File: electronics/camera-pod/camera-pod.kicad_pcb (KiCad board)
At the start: 2 copper layers, 40 x 27 mm, 16 parts, among them J1 LEAD, J2 MEGA, U1 AMS1117-3.3

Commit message: Schematic review S1, S4, S6: POS_IN 150k, the hub's ON LEDs on 18k, the camera's 0.75 A PTC
The user approved them ("S1 oui / S6 oui / S4 oui").

* S1, bay node: R29 470k -> 150k (C22807, basic).
  - Before its firmware runs, the upstream POS output (a node's IO42, the
    hub's IO10-13) floats. The BAT54S's warm leakage (about 2-3 uA at
    65 C) could then lift POS_IN through 470k to VIL.
  - Driven high through R30 + R28, 150k still gives 2.87 V, above VIH.
  - The design.py notes and bay_node.dtsi follow.
* S4, power hub: R41-R44 (the ON LEDs on the row outputs) 10k -> 18k
  (C25810, already on the board): 1.4 mA and 37 mW at 28 V. The 10k
  ran at 75 % of its 0603 rating at 29.4 V.
* S6, bay node: F1 (CAM_5V) goes from the 0.5 A PTC to SMD1206P075TF
  (RUILON, C20987, new catalog key pptc750): 0.75 A hold, 1.5 A trip,
  the same 1206 footprint. It is extended like C20799, so no fee changes.
  - Arducam gives the Mega 317 mA working: with the LEDs that is
    ~0.42 A on CAM_5V, where the 0.5 A part holds ~0.31 A at 70 C.
  - The camera pod's LDO tab gets the copper its routing leaves: a
    top-side +3V3 pour round the tab and a bottom-side island, joined by
    three vias. U1 drops ~0.5 W at 317 mA. The routing is unchanged.
  - The "~120 mA" notes go to 317 mA (node and pod design.py,
    electronics.md).
  - The bay's worst case follows: <= 2.25 A on +5V, the buck's inductor
    peaking at ~2.65 A (under its 2.9 A minimum limit), 13.5 W from
    VRACK (power-distribution-review.md, the buck notes).

The routed PCBs keep their routing.
- Node and hub: only the changed parts' properties (KiCad's Python, as
  pcbgen sets them).
- Pod: the two new zones and three vias, refilled.
- ERC 0, DRC 0, unconnected 0, parity 0 on all three (run on the Mac:
  zephyrbox didn't answer).
- keep_unchanged kept the node's renders and the hub's Gerbers. The
  hub's bottom render is restored: 9 pixels of via-hole noise, as before.
- The pod's renders, Gerbers and viewer GLB chang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
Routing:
- net +3V3: vias 0 -> 3
- added copper zone on B.Cu, net +3V3
- added copper zone on F.Cu, net +3V3
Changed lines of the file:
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@@
+	)
+	(via
+		(at 24.75 12.6)
+		(size 0.6)
+		(drill 0.3)
+		(layers "F.Cu" "B.Cu")
+		(locked yes)
+		(free yes)
+		(net "+3V3")
+	)
+	(via
+		(at 24.75 14.6)
+		(size 0.6)
+		(drill 0.3)
+		(layers "F.Cu" "B.Cu")
+		(locked yes)
+		(free yes)
+		(net "+3V3")
+	)
+	(via
+		(at 24.75 13.6)
+		(size 0.6)
+		(drill 0.3)
+		(layers "F.Cu" "B.Cu")
+		(locked yes)
+		(free yes)
+		(net "+3V3")
 	)
 	(via
@@
 			)
 		)
+	)
+	(zone
+		(net "+3V3")
+		(layer "F.Cu")
+		(name "ldo-tab")
+		(hatch edge 0.5)
+		(priority 2)
+		(connect_pads yes
+			(clearance 0.25)
+		)
+		(min_thickness 0.2)
+		(fill yes
+			(thermal_gap 0.5)
+			(thermal_bridge_width 0.5)
+			(island_removal_mode 0)
+		)
+		(polygon
+			(pts
+				(xy 21.4 10.95) (xy 25.4 10.95) (xy 25.4 16.8) (xy 21.4 16.8)
+			)
+		)
+	)
+	(zone
+		(net "+3V3")
+		(layer "B.Cu")
+		(name "ldo-tab-b")
+		(hatch edge 0.5)
+		(priority 2)
+		(connect_pads yes
+			(clearance 0.25)
+		)
+		(min_thickness 0.2)
+		(fill yes
+			(thermal_gap 0.5)
+			(thermal_bridge_width 0.5)
+			(island_removal_mode 0)
+		)
+		(polygon
+			(pts
+				(xy 22.2 11.8) (xy 27.6 11.8) (xy 27.6 17.2) (xy 22.2 17.2)
+			)
+		)

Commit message: Datasheet audit F1-F6: the pod's AP2114H, STB 5.1k, PC_DET hysteresis, the camera ESD's 100 nF, the eFuse step
The user approved the audit's fixes for the node, the hub and the pod
("Go pour 1"); docs/datasheet-audit.md marks F1-F6 applied.

* F1, camera pod: U1 AMS1117-3.3 -> AP2114H-3.3TRG1 (C150716, catalog
  ldo_1a, the node's U2).
  - The AMS1117 is specified stable only with 22 uF tantalum; the
    AP2114H is stable with the ceramic C2.
  - Same SOT-223 pinout, copper (the +3V3 pour and island round the
    tab stay) and 180 deg CPL correction.
  - One more extended type on the pod's Economic order: +$3.09 and
    $0.05 of parts (JLC_SINCE_QUOTE).
* F2, power hub: R214 (TJA1462 STB pull-down) 10k -> 5.1k (C23186,
  already on the board). With IO9 floating, STB's internal pull-up
  (20 kOhm minimum) left it at up to 1.10 V, over VIL 0.99 V.
* F3, bay node: R42 150k from MUX_SEL back to PC_DET, beside U7 (C22807,
  on the board since S1).
  - The laptop's VBUS rises at ~50 us/V through R11/R12, where the
    LVC1G32 wants <= 10 ns/V and warns of oscillation.
  - This gives ~0.14 V of hysteresis.
* F4, bay node: C28 100 nF (C14663) on U12/U13's VBUS pins (+3V3), above
  U12 by its pin 5. Between the two ICs their courtyards leave no room.
* F5, node and hub: firmware.md's first-flash procedure gains the
  irreversible DIS_USB_OTG_DOWNLOAD_MODE eFuse step. In USB-OTG
  download boot the ROM drives IO40 high: the node's DUT_FLT_N, the
  hub's PD_SCL. Nothing is burnt.
* F6, notes, hub:
  - the IMON filter is 0.9 ms, not 47 us: the pin is a current source;
  - the buck stops at ~3.8 V (internal UVLO);
  - SHDN turns on at >= 1 V;
  - the soft start stays under the limit only typically;
  - the CH224A note follows CH224 V2.1: the source PDOs are listed for
    both parts and readable under 100 W, which is still to check with
    ours (review R3); single-byte transfers; no "same die".
* F6, notes, node: TPS2553D; the LDO's 1.94 V x 0.4 A ~ 0.8 W; L1's
  7.5 A guarante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
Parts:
- U1: value AMS1117-3.3 -> AP2114H-3.3TRG1
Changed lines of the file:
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@@
 			)
 		)
-		(property "Value" "AMS1117-3.3"
+		(property "Value" "AP2114H-3.3TRG1"
 			(at 0 4.5 0)
 			(layer "F.Fab")
@@
 			)
 		)
-		(property "Datasheet" ""
+		(property "Datasheet" "https://www.diodes.com/assets/Datasheets/AP2114.pdf"
 			(at 0 0 0)
 			(unlocked yes)
@@
 			)
 		)
-		(property "Description" "3.3 V 1 A LDO"
+		(property "Description" "3.3 V 1 A LDO, 450 mV dropout at 1 A, SOT-223"
 			(at 0 0 0)
 			(unlocked yes)
@@
 			)
 		)
-		(property "MPN" "AMS1117-3.3"
+		(property "MPN" "AP2114H-3.3TRG1"
 			(at 0 0 0)
 			(layer "F.Fab")
@@
 			)
 		)
-		(property "Manufacturer" "AMS"
+		(property "Manufacturer" "Diodes Incorporated"
 			(at 0 0 0)
 			(layer "F.Fab")
@@
 			)
 		)
-		(property "LCSC" "C6186"
+		(property "LCSC" "C150716"
 			(at 0 0 0)
 			(layer "F.Fab")

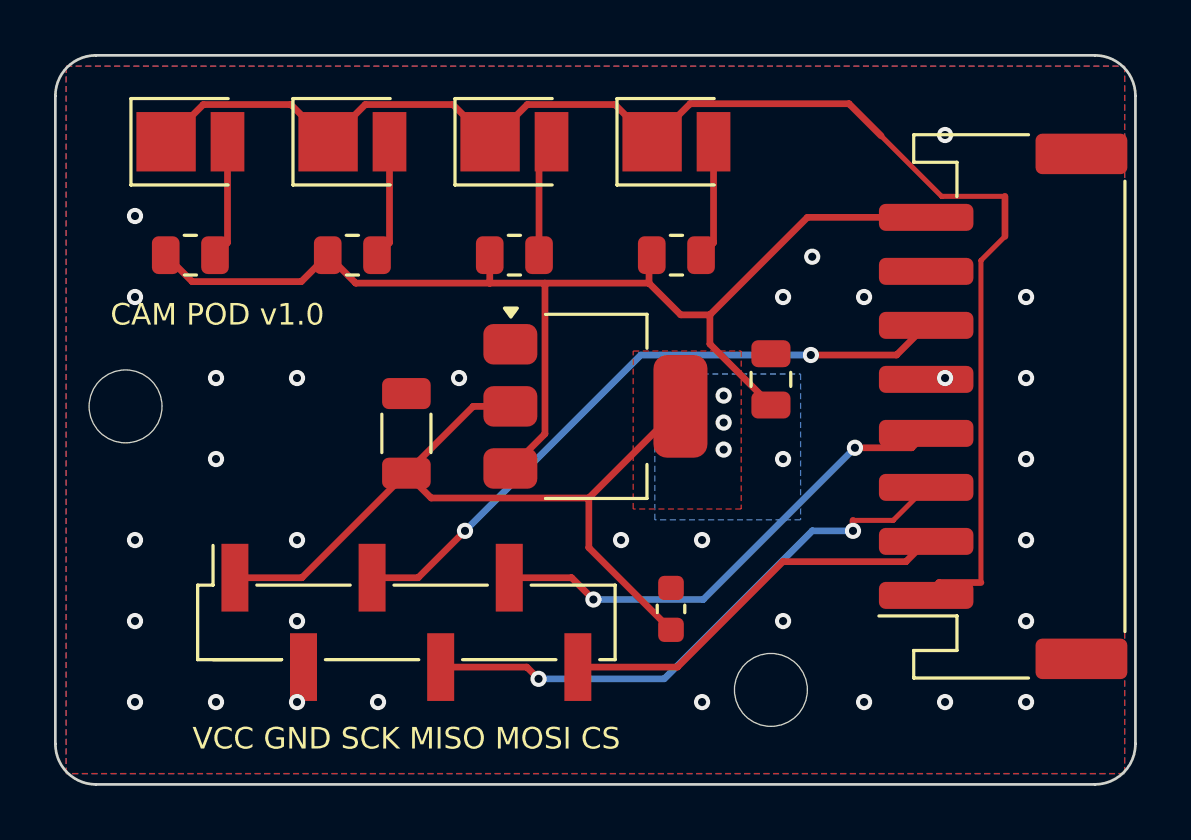
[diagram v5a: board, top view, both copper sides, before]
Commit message: Boards: labelled bottom test pads; hub dVdT 100 nF, 50 ms FLT blank
Eve's DFT rule on the four boards this session owns: bare pads on the
bottom, named on B.SilkS, out of the BOM and the CPL (no part, no
assembly fee).  Supply pads 1.5 mm, signal pads 1.0 mm (new catalog
entry "testpad1"), all more than 2 mm from any THT pad or hole
(closest: 4.7 mm, the pod's TP4).  Positions are fixed in design.py,
so they stay put across revisions.

- bay node, 17: TX, RX, 3V3, GND by the module (kept), then EN, IO0,
  FLT (DUT_FLT_N), ALRT (INA_ALERT_N), SDA, SCL and a second GND;
  a supply row along the bottom edge: GND, VIN, 5V, 3V3, DUT 5V,
  CAM 5V
- power hub, 20: TX, RX, 3V3, GND, 5V, VRACK, GND (kept), then EN,
  IO0, the CH224A's PD SDA/SCL, each row's FLT and IMON (A-D) and a
  third GND in the middle
- camera pod, 4: GND, 5V, 3V3 and a second GND at the far end
- DATA port, 2: GND and 5V (VBUS, through a via under its track)

Hub, as the datasheet audit's U1 answer asks (TPS2660 Fig. 55 at
85 C: 8-10 ms at 21 W fails the 47 nF worst start, 33 ms at 14 W
covers 100 nF): C21-C24 dVdT 47 nF -> 100 nF, so a row's soft start
is 16-22 ms and dissipates about 7-9 W typical, 14 W worst, for
19-24 ms; the firmware's HUB_ROW_FLT_BLANK_MS goes 25 -> 50 ms to
cover it (worst case 39 ms).  docs/power.md, the audit row and the
hub notes say so.

Routing fallout: J1's A12/B1 GND now leaves through one drawn 0.5 mm
via so the automatic fan-out can't cut the VRACK pour off A9/B4; the
pod's LDO tab zones are exclusive so tracks no longer split them.

All four rerouted, tidied and checked: ERC 0, DRC 0, unconnected 0,
parity 0.  Gerbers, renders, schematics, viewer GLBs, the JLC
snapshot lines and the rack BOM regenerated.

Co-Authored-By: Claude Opus 5.5 <noreply@anthropic.com>
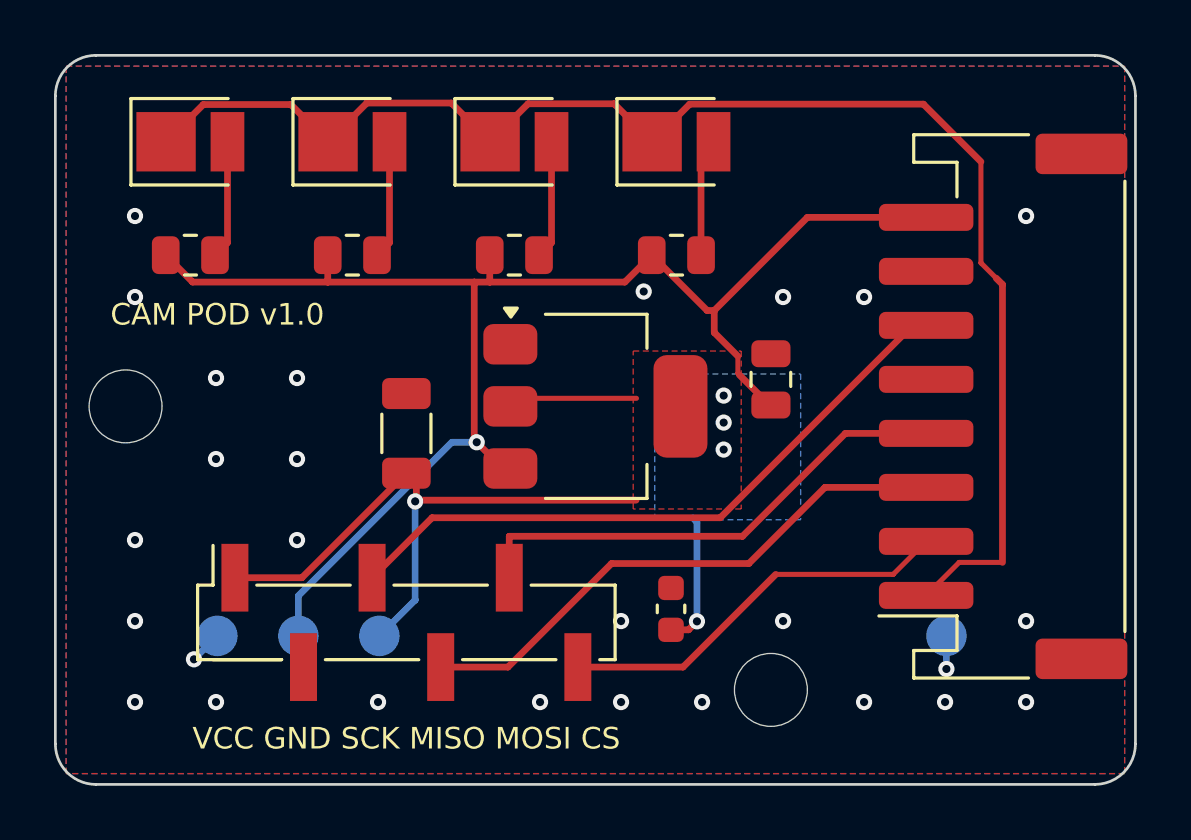
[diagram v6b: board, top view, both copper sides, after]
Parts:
- added TP1: GND, TestPoint:TestPoint_Pad_D1.5mm, B.Cu at (6.00, 21.5)
- added TP2: CAM_5V, TestPoint:TestPoint_Pad_D1.5mm, B.Cu at (9.00, 21.5)
- added TP3: +3V3, TestPoint:TestPoint_Pad_D1.5mm, B.Cu at (12.0, 21.5)
- added TP4: GND, TestPoint:TestPoint_Pad_D1.5mm, B.Cu at (33.0, 21.5)
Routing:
- net /Pod/CAM_5V: track 45.2 -> 55.7 mm, vias 0 -> 1
- net GND: track 0.00 -> 2.45 mm, vias 32 -> 27
- net +3V3: track 30.9 -> 32.6 mm, vias 3 -> 5
- net /Pod/MISO: track 21.3 -> 20.7 mm, vias 2 -> 0
- net /Pod/MOSI: track 18.3 -> 18.6 mm, vias 2 -> 0
- net /Pod/SCK: vias 2 -> 0
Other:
- board text added: "3V3"
- board text added: "5V"
- board text added: "GND"

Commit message: Camera pod: SPI and LED test pads by J1 (CP-3)
The kicad-happy review's CP-3, against Eve's rule: the pod had test
pads on its supplies only.  TP5-TP9 are bare 1.0 mm pads on B.Cu,
named on B.SilkS and kept out of the BOM and the CPL: SCK, MOSI, MISO,
CS and LED (LED_K, the LEDs' switched cathode).  They sit by J1, where
those lines come in from the node, and stay clear of the LDO's +3V3
island on B.Cu.  Each is on a new via drawn on its net's F.Cu track,
so no routing moves.  All are at least 2 mm from any through-hole pad
or hole and 2.6 mm from each other, and no label overlaps another.

Every track and via is main's.  The router added two things: a 4.5 mm
LED_K stub laid over the existing track to reach the new via, and a
40 um dot inside C1.1.  Same stitching.  ERC 0, DRC 0, unconnected 0,
parity 0.

Co-Authored-By: Claude Opus 5.5 <noreply@anthropic.com>
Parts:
- added TP5: SCK, TestPoint:TestPoint_Pad_D1.0mm, B.Cu at (29.8, 12.0)
- added TP6: MOSI, TestPoint:TestPoint_Pad_D1.0mm, B.Cu at (28.7, 14.5)
- added TP7: MISO, TestPoint:TestPoint_Pad_D1.0mm, B.Cu at (25.7, 18.8)
- added TP8: CS, TestPoint:TestPoint_Pad_D1.0mm, B.Cu at (29.5, 19.2)
- added TP9: LED_K, TestPoint:TestPoint_Pad_D1.0mm, B.Cu at (35.1, 14.3)
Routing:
- net /Pod/LED_K: track 53.6 -> 58.2 mm, vias 0 -> 1
- net /Pod/SCK: vias 0 -> 1
- net /Pod/MOSI: vias 0 -> 1
- net /Pod/MISO: vias 0 -> 1
- net /Pod/CS: vias 0 -> 1
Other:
- board text added: "CS"
- board text added: "LED"
- board text added: "MISO"
- board text added: "MOSI"
- board text added: "SCK"

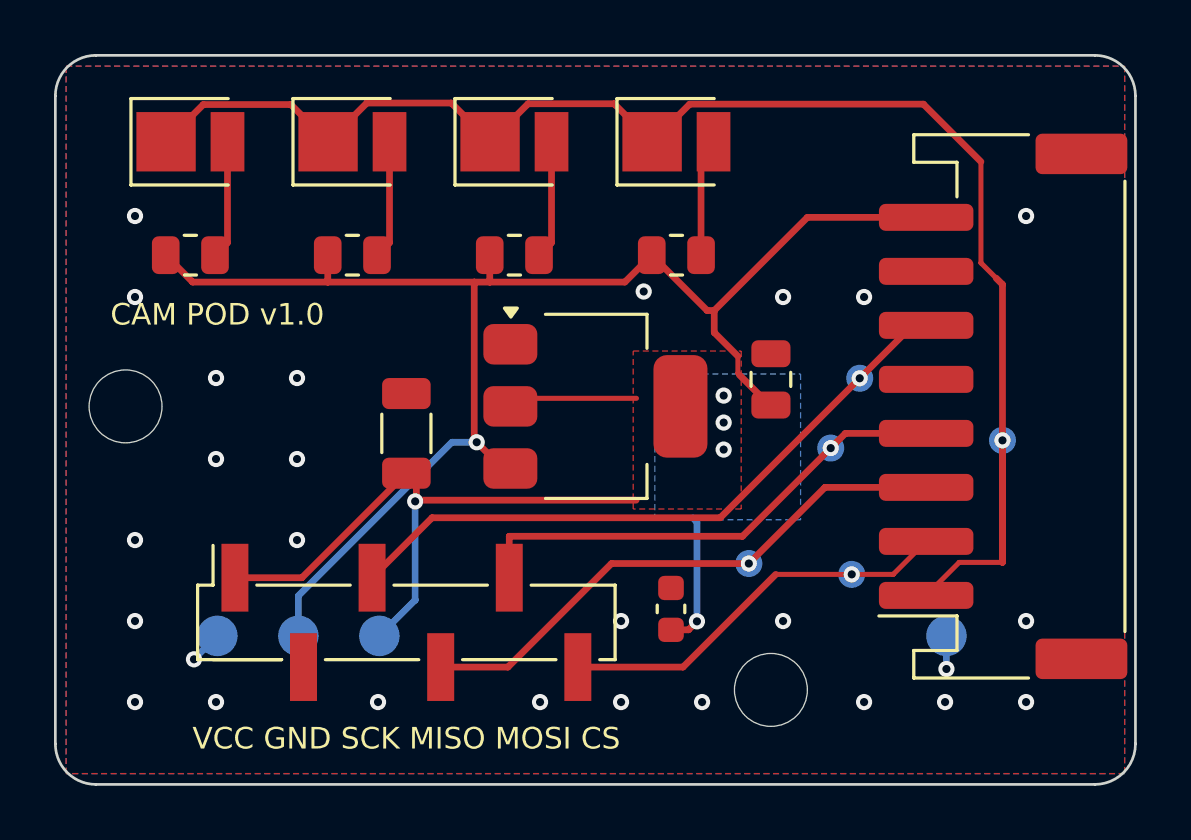
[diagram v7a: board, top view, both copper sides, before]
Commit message: Camera pod: its antennas off, a dangling track now a DRC error
tools/kicad.sh camera-pod --clean (pcbgen.clean_antennas), on the
routed board as it was, no re-route.  Four router leftovers go:
- a doubled LED_K run on F.Cu down past TP9 (LED_K's test pad): a
  track lying inside the longer one;
- two CAM_5V steps of 36 and 71 µm at C1 (U1's 10 µF input
  capacitor), folded into their neighbours;
- a 62 µm +3V3 stub inside its own via, beside C2 (U1's 22 µF
  output capacitor).
ERC, DRC (0) and connectivity are unchanged.  camera-pod leaves
electronics/antennas.json's pending list; its .kicad_pro makes a
dangling track or via an error.

Co-Authored-By: Claude Opus 5.5 <noreply@anthropic.com>
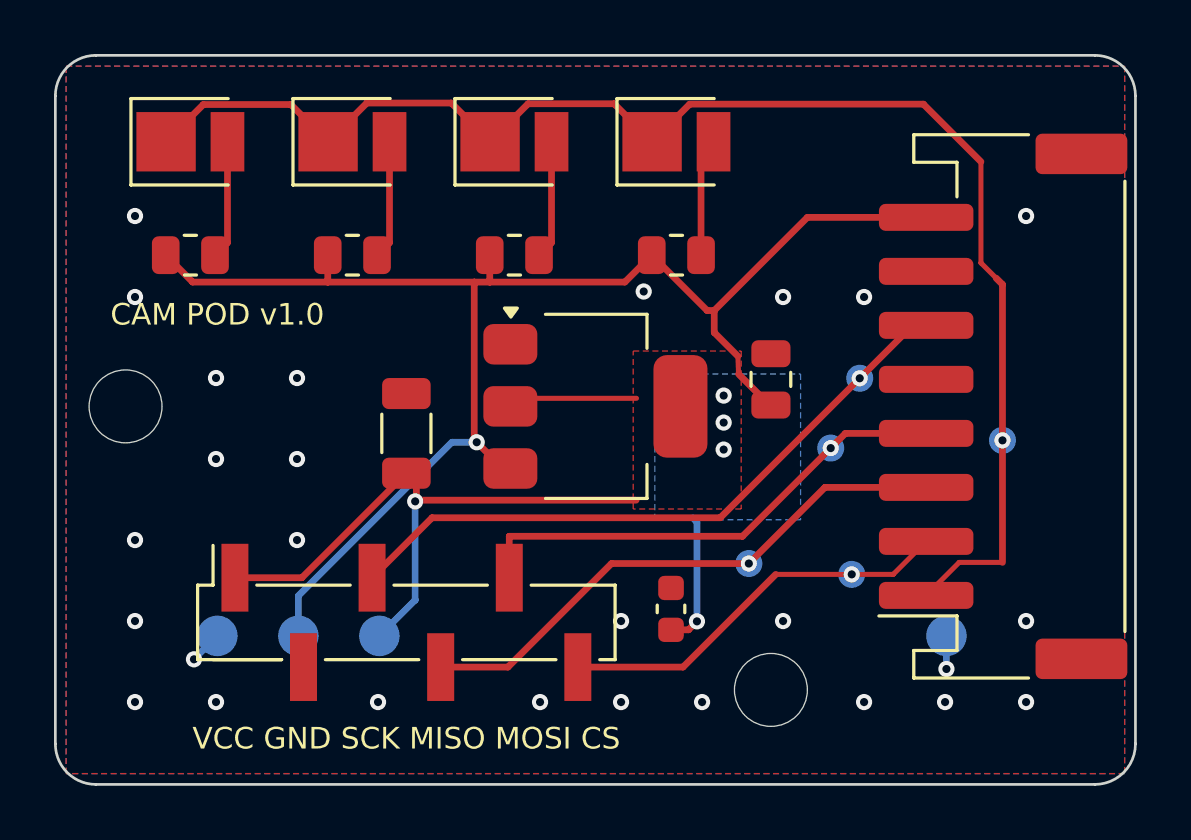
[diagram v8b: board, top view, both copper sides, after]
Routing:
- net /Pod/LED_K: track 58.2 -> 53.6 mm
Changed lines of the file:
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@@
 	)
 	(segment
-		(start 35.0758 14.2588)
+		(start 35.0758 8.4841)
 		(end 35.0758 18.7782)
 		(width 0.25)
@@
 		(end 34.8417 8.25)
 		(width 0.1874)
-		(layer "F.Cu")
-		(net "/Pod/LED_K")
-	)
-	(segment
-		(start 35.0758 8.4841)
-		(end 35.0758 18.7782)
-		(width 0.25)
 		(layer "F.Cu")
 		(net "/Pod/LED_K")
@@
 	(segment
 		(start 25.2772 11.1408)
-		(end 25.2772 11.7782)
+		(end 25.3022 11.8032)
 		(width 0.1874)
 		(layer "F.Cu")
@@
 	)
 	(segment
-		(start 26.5 12.95)
-		(end 26.4745 12.9755)
-		(width 0.25)
-		(layer "F.Cu")
-		(net "/Pod/CAM_5V")
-	)
-	(segment
-		(start 25.2772 11.7782)
-		(end 25.3272 11.8282)
-		(width 0.1874)
-		(layer "F.Cu")
-		(net "/Pod/CAM_5V")
-	)
-	(segment
 		(start 15.5133 14.2372)
 		(end 15.6045 14.3284)
@@
 	)
 	(segment
-		(start 25.3272 11.8282)
+		(start 25.3022 11.8032)
 		(end 26.4745 12.9755)
 		(width 0.25)
@@
 		(layer "F.Cu")
 		(net "+3V3")
-	)
-	(segment
-		(start 13.3697 16.4738)
-		(end 13.3259 16.5176)
-		(width 0.25)
-		(layer "F.Cu")
-		(net "+3V3")
